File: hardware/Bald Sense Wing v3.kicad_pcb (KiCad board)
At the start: 4 copper layers, 50.8 x 22.9 mm, 44 parts, among them J1 feather long, J2 feather short, J3 1140084168, Q1 Q_PNP_BEC, Q2 Q_NPN_BEC, U1 APDS-9960, U2 DS3231MZ, U3 SHT30-DIS, U4 MIC5504-3.3YM5, U5 CMM-4737DT-26186-TR

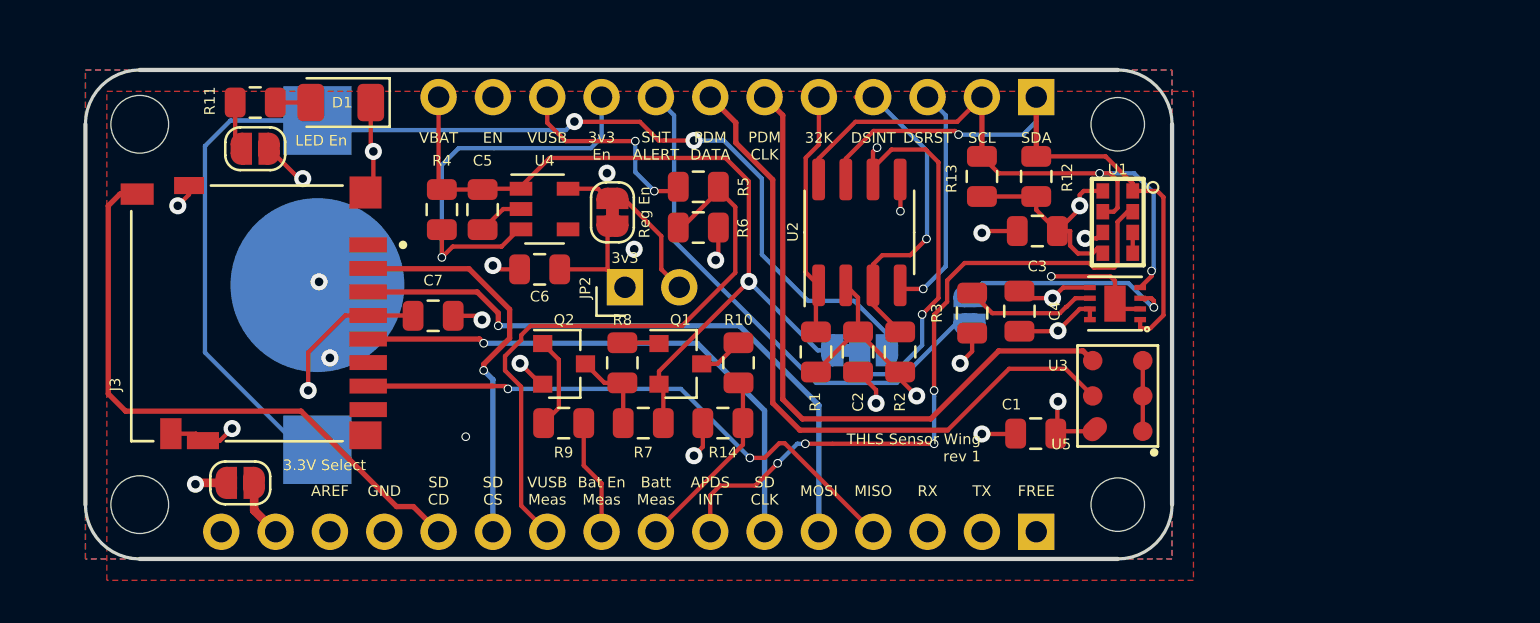
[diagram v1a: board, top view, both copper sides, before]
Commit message: changed R to 0402 and C to 0603
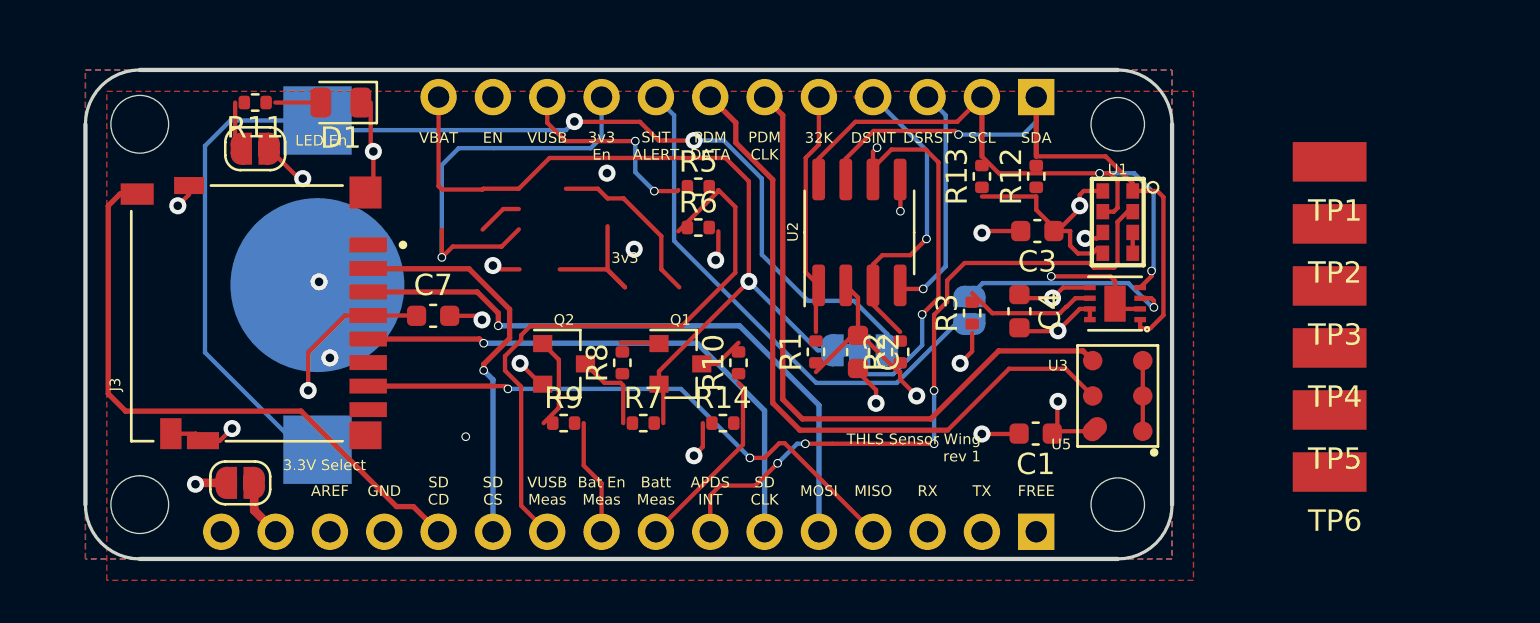
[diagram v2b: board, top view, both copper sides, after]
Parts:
- removed C5, C6: 1uF, Capacitor_SMD:C_0805_2012Metric
- removed JP2: M02, Connector_PinHeader_2.54mm:PinHeader_1x02_P2.54mm_Vertical
- removed JP4: Reg En, Jumper:SolderJumper-2_P1.3mm_Bridged_RoundedPad1.0x1.5mm
- removed R4: DNP, Resistor_SMD:R_0805_2012Metric
- removed U4: MIC5504-3.3YM5, Package_TO_SOT_SMD:SOT-23-5
- added TP1: TestPoint_Harwin, My Libraries:Harwin-S1751-46-Test-Point, F.Cu at (83.6, 29.7)
- added TP2: TestPoint_Harwin, My Libraries:Harwin-S1751-46-Test-Point, F.Cu at (83.6, 32.6)
- added TP3: TestPoint_Harwin, My Libraries:Harwin-S1751-46-Test-Point, F.Cu at (83.6, 35.5)
- added TP4: TestPoint_Harwin, My Libraries:Harwin-S1751-46-Test-Point, F.Cu at (83.6, 38.4)
- added TP5: TestPoint_Harwin, My Libraries:Harwin-S1751-46-Test-Point, F.Cu at (83.6, 41.3)
- added TP6: TestPoint_Harwin, My Libraries:Harwin-S1751-46-Test-Point, F.Cu at (83.6, 44.2)
- BT1: renamed from You can put a battery here!
- C1, C2, C3, C4, C7: footprint Capacitor_SMD:C_0805_2012Metric -> Capacitor_SMD:C_0603_1608Metric
- D1: footprint LED_SMD:LED_1206_3216Metric -> LED_SMD:LED_0805_2012Metric
- R1, R10, R11, R12, R13, R14, R2, R3, R5, R6, R7, R8, R9: footprint Resistor_SMD:R_0805_2012Metric -> Resistor_SMD:R_0402_1005Metric
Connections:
- net +3V3 renamed +3.3V
- J1 pad 1: /FREE -> /NC1
- J1 pad 10: /VUSB_Meas -> /Batt_Meas_En
- J1 pad 11: /SD_CS -> /Batt_Meas
- J1 pad 12: /SD_CD -> /VUSB_Meas
- J1 pad 14: /AREF -> /NC2
- J1 pad 7: /APDS_INT -> /SD_CS
- J1 pad 8: /Batt_Meas -> /SD_CD
- J1 pad 9: /Batt_Meas_En -> /APDS_INT
- J2 pad 9: /3v3_Reg_En -> /Load_SW_En
- J3 pad 1: Net-(J3-Pad1) -> unconnected-(J3-DATA_LINE[BIT_2]-Pad1)
- J3 pad 8: Net-(J3-Pad8) -> unconnected-(J3-DATA_LINE[BIT_1]-Pad8)
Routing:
- net /Load_SW_En: track 0.00 -> 19.6 mm, vias 0 -> 1
- net /3v3_Reg_En: track 19.6 -> 0.00 mm, vias 1 -> 0
- net (no net): track 0.00 -> 14.7 mm
- net /SD_CD: track 28.5 -> 37.2 mm
- net /Batt_Meas: track 8.73 -> 0.00 mm
- net Net-(JP2-Pad2): track 8.12 -> 0.00 mm
- net +3.3V: track 46.7 -> 40.2 mm
- net /APDS_INT: track 32.4 -> 37.8 mm
- net /Batt_Meas_En: track 5.43 -> 0.00 mm

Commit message: Cleaned up older custom symbols. Ran track clean-up on PCB.
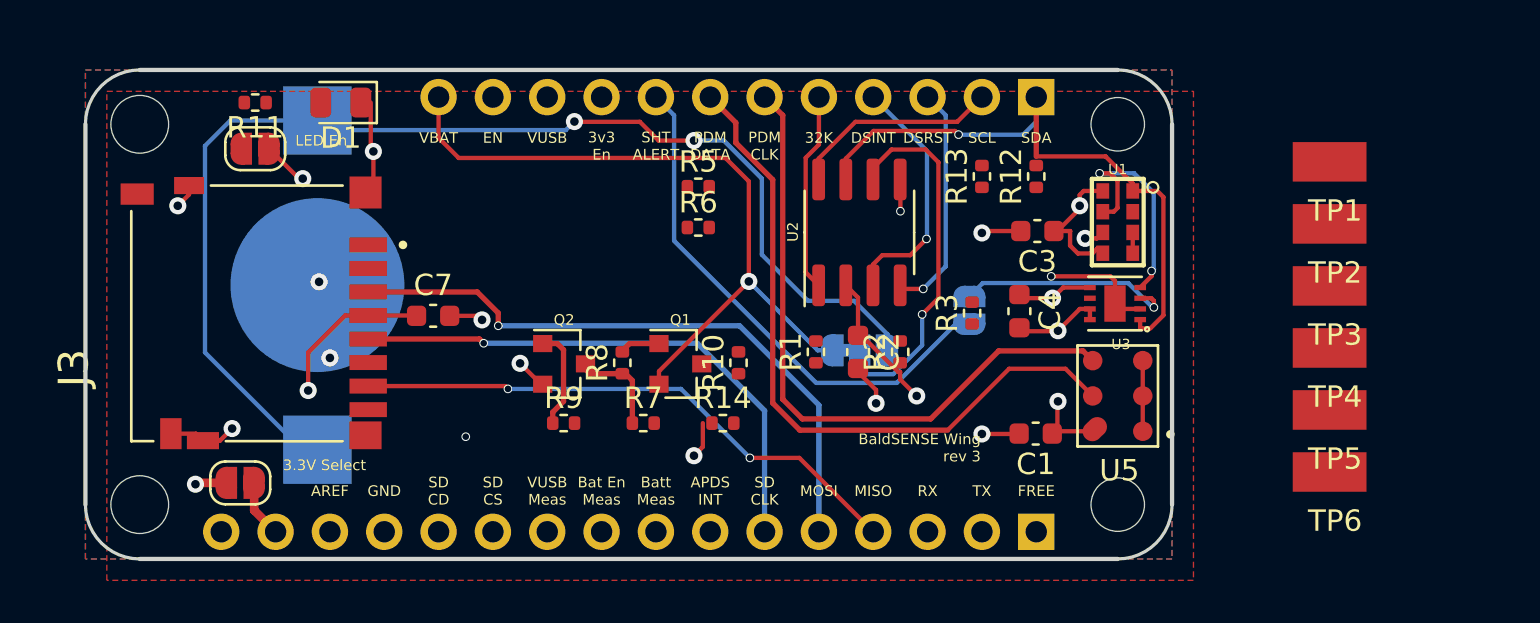
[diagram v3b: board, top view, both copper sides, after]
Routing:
- net /APDS_INT: track 37.8 -> 0.00 mm, vias 4 -> 0
- net /SD_CD: track 37.2 -> 0.00 mm
- net /VUSB_Meas: track 28.4 -> 0.00 mm
- net /Load_SW_En: track 19.6 -> 0.00 mm, vias 1 -> 0
- net /SD_CS: track 18.5 -> 0.00 mm, vias 1 -> 0
- net (no net): track 14.7 -> 0.00 mm
- net +3.3V: track 40.2 -> 30.5 mm, vias 8 -> 7
- net /VUSB: track 9.52 -> 0.00 mm, vias 2 -> 0
- net /SCL: track 29.0 -> 20.4 mm
- net GND: track 39.3 -> 32.9 mm, vias 20 -> 16
- net Net-(U3-~{RESET}): track 6.19 -> 0.00 mm
- net /VBAT: track 38.1 -> 33.7 mm
- net /DS3231_INT: track 15.2 -> 11.7 mm
- net Net-(JP5-B): track 2.28 -> 0.00 mm
- net /32KHz: track 11.5 -> 9.31 mm
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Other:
- board text added: "BaldSENSE Wing james@baldengineer.com Rev 3"
- board text added: "BaldSENSE Wing rev 3"
- board text removed: "3v3"
- board text removed: "THLS Sensor Wing james@baldengineer.com Rev1 Hi to everyone who helped on the Twitch Stream!"
- board text removed: "THLS Sensor Wing rev 1"

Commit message: updated pin header silk
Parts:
- moved J3 9.83 mm to (27.9, 37.1), turned to -90 degrees
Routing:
- net +3.3V: track 30.5 -> 20.9 mm, vias 7 -> 5
- net /SD_DIn: track 29.5 -> 22.4 mm
- net /SD_DOut: track 26.4 -> 19.8 mm
- net /SD_CLK: track 25.6 -> 20.4 mm
- net GND: track 32.9 -> 29.0 mm, vias 16 -> 13
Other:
- board text added: "NC1"
- board text added: "NC2"
- board text added: "Wing En"
- board text removed: "3v3 En"
- board text removed: "AREF"
- board text removed: "FREE"

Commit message: added load switch and changed power markers
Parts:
- added R15: 10K, Resistor_SMD:R_0402_1005Metric, F.Cu at (50.2, 35.1)
- added R4: 10K, Resistor_SMD:R_0402_1005Metric, F.Cu at (50.2, 33.1)
- added TP7: TestPoint_Harwin, My Libraries:Harwin-S1751-46-Test-Point, F.Cu at (89.5, 43.0)
- added U4: AP2151AW-7, Package_TO_SOT_SMD:SOT-23-5, F.Cu at (46.1, 34.6)
- R12, R13: value 4.7K -> 10K
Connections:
- net /3v3_feather renamed +3v3_Feather
- net /VUSB renamed +Vusb
- J2 pad 12: /VBAT -> +Vbatt
- Q1 pad 2: /VBAT -> +Vbatt
- R7 pad 2: /VBAT -> +Vbatt
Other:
- board text added: "Remove Silks Add Something fun on the power layer"

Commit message: 14 unrouted
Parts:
- added J4: STEMMA-QT, Connector_JST:JST_SH_BM04B-SRSS-TB_1x04-1MP_P1.00mm_Vertical, F.Cu at (54.2, 33.7)
- added JP2: RTC Batt Select, Jumper:SolderJumper-3_P1.3mm_Bridged12_RoundedPad1.0x1.5mm, B.Cu at (67.8, 40.0)
- added R16: 10K, Resistor_SMD:R_0402_1005Metric, F.Cu at (67.6, 32.6)
- added SW1: PTS810, Button_Switch_SMD:SW_SPST_PTS810, F.Cu at (42.1, 44.0)
- added TP8: Test Point, TestPoint:TestPoint_Pad_1.0x1.0mm, F.Cu at (44.5, 28.6)
- C7: moved to B.Cu
- R1, R2, R3, R5, R6: value 4.7K -> 10K
- TP1, TP6: value TestPoint_Harwin -> Test Point; footprint My Libraries:Harwin-S1751-46-Test-Point -> TestPoint:TestPoint_Pad_1.0x1.0mm
- TP2, TP3, TP4, TP5: value TestPoint_Harwin -> Test Point; footprint My Libraries:Harwin-S1751-46-Test-Point -> TestPoint:TestPoint_Pad_1.0x1.0mm; moved to B.Cu
- TP7: value TestPoint_Harwin -> FLG; footprint My Libraries:Harwin-S1751-46-Test-Point -> TestPoint:TestPoint_Pad_1.0x1.0mm
- moved TP1 49.1 mm to (36.8, 44.8)
- moved TP7 46.9 mm to (42.9, 37.8)
- moved TP6 35.5 mm to (50.2, 32.0)
- moved TP5 26.5 mm to (57.1, 39.7), turned to 180 degrees
- moved TP2 22.0 mm to (64.8, 44.1), turned to 90 degrees
- moved TP3 18.4 mm to (67.3, 44.1), turned to -90 degrees
- moved TP4 14.9 mm to (69.8, 44.1), turned to -90 degrees
- moved C7 11.8 mm to (29.9, 36.0), turned to 90 degrees
- moved R15 7.41 mm to (42.8, 36.2)
- moved R4 6.00 mm to (45.0, 36.2), turned to 180 degrees
- moved R5 5.88 mm to (48.2, 31.5)
- moved R6 5.85 mm to (48.2, 32.5), turned to 180 degrees
- moved R3 3.45 mm to (69.1, 34.1)
- moved R11 2.87 mm to (36.2, 26.7), turned to -90 degrees
- moved JP5 2.48 mm to (33.9, 26.7), turned to 0 degrees
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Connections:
- net +BATT renamed +RTC_BATT
- net /RTC_BATT renamed +V_RTC
- JP6 pad 1: /VBAT -> +Vbatt
- R3 pad 1: +3.3V -> Net-(U3-~{RESET})
- R3 pad 2: Net-(U3-~{RESET}) -> +3.3V
- U5 pad 2: GND -> Net-(JP2-C)
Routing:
- net +RTC_BATT: track 55.1 -> 0.00 mm, vias 2 -> 0
- net /APDS_INT: track 0.00 -> 44.2 mm, vias 0 -> 3
- net /VBAT: track 33.7 -> 0.00 mm, vias 1 -> 0
- net /SD_CS: track 0.00 -> 30.8 mm
- net /VUSB_Meas: track 0.00 -> 22.3 mm, vias 0 -> 1
- net /SD_DOut: track 19.8 -> 40.9 mm
- net /Batt_Meas: track 0.00 -> 18.2 mm, vias 0 -> 2
- net /SD_CD: track 0.00 -> 17.2 mm
- net /SD_CLK: track 20.4 -> 35.5 mm
- net /Load_SW_En: track 0.00 -> 14.6 mm
- net /~{RST}: track 0.00 -> 14.4 mm, vias 0 -> 1
- net +3.3V: track 20.9 -> 35.0 mm, vias 5 -> 11
- net /SD_DIn: track 22.4 -> 36.3 mm
- net Net-(JP2-C): track 0.00 -> 11.0 mm, vias 0 -> 1
- net GND: track 29.0 -> 40.0 mm, vias 13 -> 18
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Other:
- board text added: "Remove Silks Add Something fun on the power layer Add Silk for I2C Add Silk for Jumpers"
- board text removed: "Remove Silks Add Something fun on the power layer"

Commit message: working on voltage rails
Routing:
- net +3v3_Feather: track 2.70 -> 38.9 mm, vias 0 -> 2
- net +RTC_BATT: track 0.00 -> 33.8 mm, vias 0 -> 4
- net +Vbatt: track 0.86 -> 26.9 mm, vias 0 -> 2
- net +Vusb: track 0.00 -> 5.12 mm, vias 0 -> 1
- net +V_RTC: track 17.4 -> 16.1 mm
- added copper zone on In2.Cu, net +RTC_BATT

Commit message: first to 0 unrouted!
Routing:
- net /SDA: track 29.2 -> 47.1 mm, vias 3 -> 4
- net +Vbatt: track 26.9 -> 10.8 mm
- net +3v3_Feather: track 38.9 -> 23.0 mm
- net /SCL: track 29.8 -> 36.9 mm
- net /APDS_INT: track 44.2 -> 39.8 mm
- net Net-(JP3-A): track 11.7 -> 16.0 mm
- net /VUSB_Meas: track 22.3 -> 19.9 mm
- net /Batt_Meas: track 18.2 -> 20.3 mm, vias 2 -> 1
- net +RTC_BATT: track 33.8 -> 35.9 mm, vias 4 -> 2
- net /SHT30_ALERT: track 24.8 -> 22.8 mm
- net Net-(Q1-C): track 0.00 -> 1.97 mm
- net +V_RTC: track 16.1 -> 15.1 mm
- net +3.3V: track 35.4 -> 36.3 mm, vias 11 -> 12
- net Net-(JP2-C): track 11.0 -> 10.5 mm
- net GND: track 40.0 -> 39.7 mm, vias 18 -> 21
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- added copper zone on B.Cu, net +RTC_BATT
- added copper zone on B.Cu, net +Vbatt
- removed copper zone on In2.Cu, net +RTC_BATT
- removed copper zone on B.Cu, net GND
